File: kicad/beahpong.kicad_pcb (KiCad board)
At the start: 2 copper layers, 65 x 56 mm, 16 parts, among them J1 Conn_02x20_Odd_Even, J2 Conn_01x02, J3 Screw_Terminal_01x02, Q1 DMG2305UX, U1 CAT24C32, U2 DMMT5401

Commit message: Add level shifters
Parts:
- added C2: 100n, Capacitor_SMD:C_0402_1005Metric, F.Cu at (-20.9, -34.5)
- added C3: 100n, Capacitor_SMD:C_0402_1005Metric, F.Cu at (-22.0, -31.9)
- added C4: 100n, Capacitor_SMD:C_0402_1005Metric, F.Cu at (-26.0, -29.4)
- added R10: 680, Resistor_SMD:R_0603_1608Metric, F.Cu at (33.0, 39.5)
- added R11: 680, Resistor_SMD:R_0603_1608Metric, F.Cu at (-32.0, -44.2)
- added R12: 680, Resistor_SMD:R_0603_1608Metric, F.Cu at (35.0, 39.5)
- added R13: 680, Resistor_SMD:R_0603_1608Metric, F.Cu at (-36.4, -39.7)
- added R14: 680, Resistor_SMD:R_0603_1608Metric, F.Cu at (37.0, 39.5)
- added R15: 680, Resistor_SMD:R_0603_1608Metric, F.Cu at (-44.0, 15.0)
- added R16: 680, Resistor_SMD:R_0603_1608Metric, F.Cu at (39.0, 39.5)
- added R17: 680, Resistor_SMD:R_0603_1608Metric, F.Cu at (-32.4, -41.7)
- added R18: 680, Resistor_SMD:R_0603_1608Metric, F.Cu at (41.0, 39.5)
- added R19: 680, Resistor_SMD:R_0603_1608Metric, F.Cu at (-36.4, -37.2)
- added R20: 680, Resistor_SMD:R_0603_1608Metric, F.Cu at (43.0, 39.5)
- added R21: 680, Resistor_SMD:R_0603_1608Metric, F.Cu at (-44.0, 12.5)
- added R22: 200K, Resistor_SMD:R_0603_1608Metric, F.Cu at (43.5, 55.5)
- added R23: 200K, Resistor_SMD:R_0603_1608Metric, F.Cu at (-32.4, -39.2)
- added R24: 680, Resistor_SMD:R_0603_1608Metric, F.Cu at (41.5, 55.5)
- added R25: 680, Resistor_SMD:R_0603_1608Metric, F.Cu at (-19.0, 12.0)
- added R26: 680, Resistor_SMD:R_0603_1608Metric, F.Cu at (39.5, 55.5)
- added R27: 680, Resistor_SMD:R_0603_1608Metric, F.Cu at (-19.0, 14.0)
- added R28: 680, Resistor_SMD:R_0603_1608Metric, F.Cu at (37.5, 55.5)
- added R29: 680, Resistor_SMD:R_0603_1608Metric, F.Cu at (-24.0, -44.2)
- added R30: 680, Resistor_SMD:R_0603_1608Metric, F.Cu at (35.5, 55.5)
- added R31: 680, Resistor_SMD:R_0603_1608Metric, F.Cu at (-28.4, -39.2)
- added R32: 680, Resistor_SMD:R_0603_1608Metric, F.Cu at (33.5, 55.5)
- added R33: 680, Resistor_SMD:R_0603_1608Metric, F.Cu at (-24.0, 15.5)
- added R34: 680, Resistor_SMD:R_0603_1608Metric, F.Cu at (31.5, 55.5)
- added R35: 680, Resistor_SMD:R_0603_1608Metric, F.Cu at (-24.4, -41.7)
- added R36: 680, Resistor_SMD:R_0603_1608Metric, F.Cu at (29.5, 55.5)
- added R37: 680, Resistor_SMD:R_0603_1608Metric, F.Cu at (-28.4, -36.7)
- added R38: 680, Resistor_SMD:R_0603_1608Metric, F.Cu at (27.5, 55.5)
- added R39: 680, Resistor_SMD:R_0603_1608Metric, F.Cu at (-24.0, 17.5)
- added R40: 680, Resistor_SMD:R_0603_1608Metric, F.Cu at (-24.4, -39.2)
- added R41: 680, Resistor_SMD:R_0603_1608Metric, F.Cu at (-43.0, 6.50)
- added R42: 680, Resistor_SMD:R_0603_1608Metric, F.Cu at (-33.5, -29.2)
- added R43: 680, Resistor_SMD:R_0603_1608Metric, F.Cu at (-28.4, -34.2)
- added R44: 680, Resistor_SMD:R_0603_1608Metric, F.Cu at (-20.3, -41.7)
- added R45: 680, Resistor_SMD:R_0603_1608Metric, F.Cu at (-29.5, -31.7)
- added R46: 680, Resistor_SMD:R_0603_1608Metric, F.Cu at (-43.0, 4.50)
- added R47: 680, Resistor_SMD:R_0603_1608Metric, F.Cu at (-43.0, 2.50)
- added R48: 200K, Resistor_SMD:R_0603_1608Metric, F.Cu at (-15.0, -4.50)
- added R49: 680, Resistor_SMD:R_0603_1608Metric, F.Cu at (-20.3, -39.2)
- added R50: 680, Resistor_SMD:R_0603_1608Metric, F.Cu at (-15.0, 0.50)
- added R51: 680, Resistor_SMD:R_0603_1608Metric, F.Cu at (-15.0, 2.50)
- added R52: 680, Resistor_SMD:R_0603_1608Metric, F.Cu at (-24.4, -34.2)
- added R53: 680, Resistor_SMD:R_0603_1608Metric, F.Cu at (-15.0, 6.00)
- added R54: 680, Resistor_SMD:R_0603_1608Metric, F.Cu at (-25.5, -31.7)
- added R55: 680, Resistor_SMD:R_0603_1608Metric, F.Cu at (-20.3, -36.7)
- added R56: 680, Resistor_SMD:R_0603_1608Metric, F.Cu at (-23.5, 8.50)
- added R6: 680, Resistor_SMD:R_0603_1608Metric, F.Cu at (29.0, 39.5)
- added R7: 680, Resistor_SMD:R_0603_1608Metric, F.Cu at (-40.4, -38.7)
- added R8: 680, Resistor_SMD:R_0603_1608Metric, F.Cu at (31.0, 39.5)
- added R9: 680, Resistor_SMD:R_0603_1608Metric, F.Cu at (-44.0, 17.5)
- added U3: NVT2008PW, Package_SO:TSSOP-20_4.4x6.5mm_P0.65mm, F.Cu at (36.5, 47.5)
- added U4: NVT2008PW, Package_SO:TSSOP-20_4.4x6.5mm_P0.65mm, F.Cu at (-32.5, 14.5)
- added U5: NVT2008PW, Package_SO:TSSOP-20_4.4x6.5mm_P0.65mm, F.Cu at (-32.5, 4.00)
- J3: footprint Connector_Phoenix_MC:PhoenixContact_MCV_1,5_2-G-3.5_1x02_P3.50mm_Vertical -> Connector_Molex:Molex_KK-254_AE-6410-02A_1x02_P2.54mm_Vertical
- U1: value CAT24C32 -> DMMT5401; footprint Package_SO:SOIC-8_3.9x4.9mm_P1.27mm -> Package_TO_SOT_SMD:SOT-23-6
- U2: value DMMT5401 -> CAT24C32WI−GT3; footprint Package_TO_SOT_SMD:SOT-23-6 -> Package_SO:SOIC-8_3.9x4.9mm_P1.27mm
- moved U1 33.5 mm to (32.0, 30.0)
- moved U2 33.5 mm to (65.5, 29.5)
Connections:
- U1 pad 1: GND -> Net-(R4-Pad1)
- U1 pad 2: GND -> Net-(R4-Pad1)
- U1 pad 3: GND -> Net-(R4-Pad1)
- U1 pad 4: GND -> Net-(Q1-Pad1)
- U1 pad 5: /ID_SD -> +5V
- U1 pad 6: /ID_SC -> Net-(J3-Pad1)
- U2 pad 1: Net-(R4-Pad1) -> GND
- U2 pad 2: Net-(R4-Pad1) -> GND
- U2 pad 3: Net-(R4-Pad1) -> GND
- U2 pad 4: Net-(Q1-Pad1) -> GND
- U2 pad 5: +5V -> /ID_SD
- U2 pad 6: Net-(J3-Pad1) -> /ID_SC

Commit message: Finished layout of pcb
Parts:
- added J4: Conn_01x03, Connector_PinHeader_2.54mm:PinHeader_1x03_P2.54mm_Vertical, F.Cu at (77.5, 61.5)
- added J5: Conn_01x03, Connector_PinHeader_2.54mm:PinHeader_1x03_P2.54mm_Vertical, F.Cu at (77.5, 57.5)
- added J6: Conn_01x03, Connector_PinHeader_2.54mm:PinHeader_1x03_P2.54mm_Vertical, F.Cu at (77.5, 65.5)
- added J7: Conn_01x03, Connector_PinHeader_2.54mm:PinHeader_1x03_P2.54mm_Vertical, F.Cu at (77.5, 53.5)
- added J8: Conn_02x12_Odd_Even, Connector_PinHeader_2.54mm:PinHeader_2x12_P2.54mm_Vertical, F.Cu at (29.5, 72.5)
- J3: footprint Connector_Molex:Molex_KK-254_AE-6410-02A_1x02_P2.54mm_Vertical -> Connector_Phoenix_MC:PhoenixContact_MC_1,5_2-G-3.5_1x02_P3.50mm_Horizontal
- moved C4 134.5 mm to (84.2, 47.5), turned to 270 degrees
- moved R47 130.9 mm to (83.0, 38.0), turned to 270 degrees
- moved R45 129.4 mm to (79.5, 38.0), turned to 270 degrees
- moved R46 128.7 mm to (81.2, 38.0), turned to 270 degrees
- moved R23 128.6 mm to (57.8, 52.5), turned to 90 degrees
- moved R42 127.0 mm to (74.2, 38.0), turned to 270 degrees
- moved R55 126.9 mm to (73.8, 48.5), turned to 90 degrees
- moved R43 126.9 mm to (76.0, 38.0), turned to 270 degrees
- moved R44 126.4 mm to (77.8, 38.0), turned to 270 degrees
- moved R54 126.2 mm to (72.0, 48.5), turned to 90 degrees
- moved R52 124.3 mm to (68.5, 48.5), turned to 90 degrees
- moved R29 123.3 mm to (52.5, 52.5), turned to 90 degrees
- moved R40 122.5 mm to (70.8, 38.0), turned to 270 degrees
- moved R49 121.2 mm to (63.2, 48.5), turned to 90 degrees
- moved R31 121.1 mm to (50.8, 52.5), turned to 90 degrees
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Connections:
- net Net-(R24-Pad2) renamed /SENSOR_P2_3
- net Net-(R25-Pad2) renamed /SENSOR_P1_2
- net Net-(R26-Pad2) renamed /SENSOR_P1_6
- net Net-(R27-Pad2) renamed /SENSOR_P2_7
- net Net-(R28-Pad2) renamed /SENSOR_P2_2
- net Net-(R29-Pad2) renamed /SENSOR_P1_3
- net Net-(R30-Pad2) renamed /SENSOR_P1_7
- net Net-(R31-Pad2) renamed /SENSOR_P2_6
- net Net-(R32-Pad2) renamed /SENSOR_P2_1
- net Net-(R33-Pad2) renamed /SENSOR_P1_4
- net Net-(R34-Pad2) renamed /SENSOR_P1_8
- net Net-(R35-Pad2) renamed /SENSOR_P2_5
- net Net-(R36-Pad2) renamed /SENSOR_P2_0
- net Net-(R37-Pad2) renamed /SENSOR_P1_5
- net Net-(R38-Pad2) renamed /SENSOR_P1_9
- net Net-(R39-Pad2) renamed /SENSOR_P2_4
- net Net-(R49-Pad2) renamed /DOUT_M
- net Net-(R50-Pad2) renamed /DOUT_P1
- net Net-(R51-Pad2) renamed /DOUT_P2
- net Net-(R52-Pad2) renamed /RESERVED
- net Net-(R53-Pad2) renamed /SENSOR_P2_8
- net Net-(R54-Pad2) renamed /SENSOR_P1_1
- net Net-(R55-Pad2) renamed /SENSOR_P2_9
- net Net-(R56-Pad2) renamed /SENSOR_P1_0
- C2 pad 2: +5V -> Net-(C2-Pad2)
- C3 pad 2: +5V -> Net-(C3-Pad2)
- C4 pad 2: +5V -> Net-(C4-Pad2)
- J1 pad 10: (no net) -> /BCM15
- J1 pad 11: (no net) -> /BCM17
- J1 pad 12: (no net) -> /BCM18
- J1 pad 13: (no net) -> /BCM27
- J1 pad 15: (no net) -> /BCM22
- J1 pad 16: (no net) -> /BCM23
- J1 pad 18: (no net) -> /BCM24
- J1 pad 19: (no net) -> /BCM10
- J1 pad 21: (no net) -> /BCM9
- J1 pad 22: (no net) -> /BCM25
- J1 pad 23: (no net) -> /BCM11
- J1 pad 24: (no net) -> /BCM8
- J1 pad 3: (no net) -> /BCM2
- J1 pad 31: (no net) -> /BCM6
- J1 pad 32: (no net) -> /BCM12
- J1 pad 33: (no net) -> /BCM13
- J1 pad 35: (no net) -> /BCM19
- J1 pad 36: (no net) -> /BCM16
- J1 pad 37: (no net) -> /BCM26
- J1 pad 38: (no net) -> /BCM20
- J1 pad 40: (no net) -> /BCM21
- J1 pad 5: (no net) -> /BCM3
- J1 pad 7: (no net) -> /BCM4
- J1 pad 8: (no net) -> /BCM14
- R10 pad 2: Net-(R10-Pad2) -> /BCM4
- R11 pad 2: Net-(R11-Pad2) -> /BCM24
- R12 pad 2: Net-(R12-Pad2) -> /BCM14
- R13 pad 2: Net-(R13-Pad2) -> /BCM10
- R14 pad 2: Net-(R14-Pad2) -> /BCM15
- R15 pad 2: Net-(R15-Pad2) -> /BCM25
- R16 pad 2: Net-(R16-Pad2) -> /BCM17
- R17 pad 2: Net-(R17-Pad2) -> /BCM9
- R18 pad 2: Net-(R18-Pad2) -> /BCM18
- R19 pad 2: Net-(R19-Pad2) -> /BCM8
- R20 pad 2: Net-(R20-Pad2) -> /BCM27
- R21 pad 2: Net-(R21-Pad2) -> /BCM11
- R22 pad 2: Net-(R22-Pad2) -> Net-(C2-Pad2)
- R23 pad 2: Net-(R23-Pad2) -> Net-(C3-Pad2)
- R40 pad 2: Net-(R40-Pad2) -> /BCM6
- R41 pad 2: Net-(R41-Pad2) -> /BCM12
- R42 pad 2: Net-(R42-Pad2) -> /BCM13
- R43 pad 2: Net-(R43-Pad2) -> /BCM19
- R44 pad 2: Net-(R44-Pad2) -> /BCM16
- R45 pad 2: Net-(R45-Pad2) -> /BCM26
- R46 pad 2: Net-(R46-Pad2) -> /BCM20
- R47 pad 2: Net-(R47-Pad2) -> /BCM21
- R48 pad 2: Net-(R48-Pad2) -> Net-(C4-Pad2)
- R6 pad 2: Net-(R6-Pad2) -> /BCM2
- R7 pad 2: Net-(R7-Pad2) -> /BCM23
- R8 pad 2: Net-(R8-Pad2) -> /BCM3
- R9 pad 2: Net-(R9-Pad2) -> /BCM22
- U3 pad 10: Net-(R6-Pad2) -> /BCM2
- U3 pad 19: Net-(R22-Pad2) -> Net-(C2-Pad2)
- U3 pad 20: Net-(R22-Pad2) -> Net-(C2-Pad2)
- U3 pad 3: Net-(R20-Pad2) -> /BCM27
- U3 pad 4: Net-(R18-Pad2) -> /BCM18
- U3 pad 5: Net-(R16-Pad2) -> /BCM17
- U3 pad 6: Net-(R14-Pad2) -> /BCM15
- U3 pad 7: Net-(R12-Pad2) -> /BCM14
- U3 pad 8: Net-(R10-Pad2) -> /BCM4
- U3 pad 9: Net-(R8-Pad2) -> /BCM3
- U4 pad 10: Net-(R7-Pad2) -> /BCM23
- U4 pad 19: Net-(R23-Pad2) -> Net-(C3-Pad2)
- U4 pad 20: Net-(R23-Pad2) -> Net-(C3-Pad2)
- U4 pad 3: Net-(R21-Pad2) -> /BCM11
- U4 pad 4: Net-(R19-Pad2) -> /BCM8
- U4 pad 5: Net-(R17-Pad2) -> /BCM9
- U4 pad 6: Net-(R15-Pad2) -> /BCM25
- U4 pad 7: Net-(R13-Pad2) -> /BCM10
- U4 pad 8: Net-(R11-Pad2) -> /BCM24
- U4 pad 9: Net-(R9-Pad2) -> /BCM22
- U5 pad 10: Net-(R40-Pad2) -> /BCM6
- U5 pad 19: Net-(R48-Pad2) -> Net-(C4-Pad2)
- U5 pad 20: Net-(R48-Pad2) -> Net-(C4-Pad2)
- U5 pad 3: Net-(R47-Pad2) -> /BCM21
- U5 pad 4: Net-(R46-Pad2) -> /BCM20
- U5 pad 5: Net-(R45-Pad2) -> /BCM26
- U5 pad 6: Net-(R44-Pad2) -> /BCM16
- U5 pad 7: Net-(R43-Pad2) -> /BCM19
- U5 pad 8: Net-(R42-Pad2) -> /BCM13
- U5 pad 9: Net-(R41-Pad2) -> /BCM12
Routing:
- net +5V: track 16.9 -> 253.4 mm, vias 0 -> 30
- net +3V3: track 7.19 -> 143.3 mm, vias 0 -> 25
- net /DOUT_M: track 0.00 -> 44.8 mm
- net /SENSOR_P1_1: track 0.00 -> 41.4 mm
- net /SENSOR_P2_8: track 0.00 -> 40.7 mm
- net /DOUT_P1: track 0.00 -> 37.9 mm
- net /SENSOR_P2_9: track 0.00 -> 36.5 mm
- net /SENSOR_P1_0: track 0.00 -> 36.1 mm
- net /SENSOR_P1_9: track 0.00 -> 31.8 mm
- net /SENSOR_P1_5: track 0.00 -> 31.7 mm
- net /SENSOR_P1_8: track 0.00 -> 30.4 mm
- net /SENSOR_P1_4: track 0.00 -> 30.1 mm
- net /SENSOR_P2_4: track 0.00 -> 28.8 mm
- net /SENSOR_P2_0: track 0.00 -> 28.6 mm
- net /SENSOR_P1_3: track 0.00 -> 28.3 mm
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- added copper zone on B.Cu, net GND

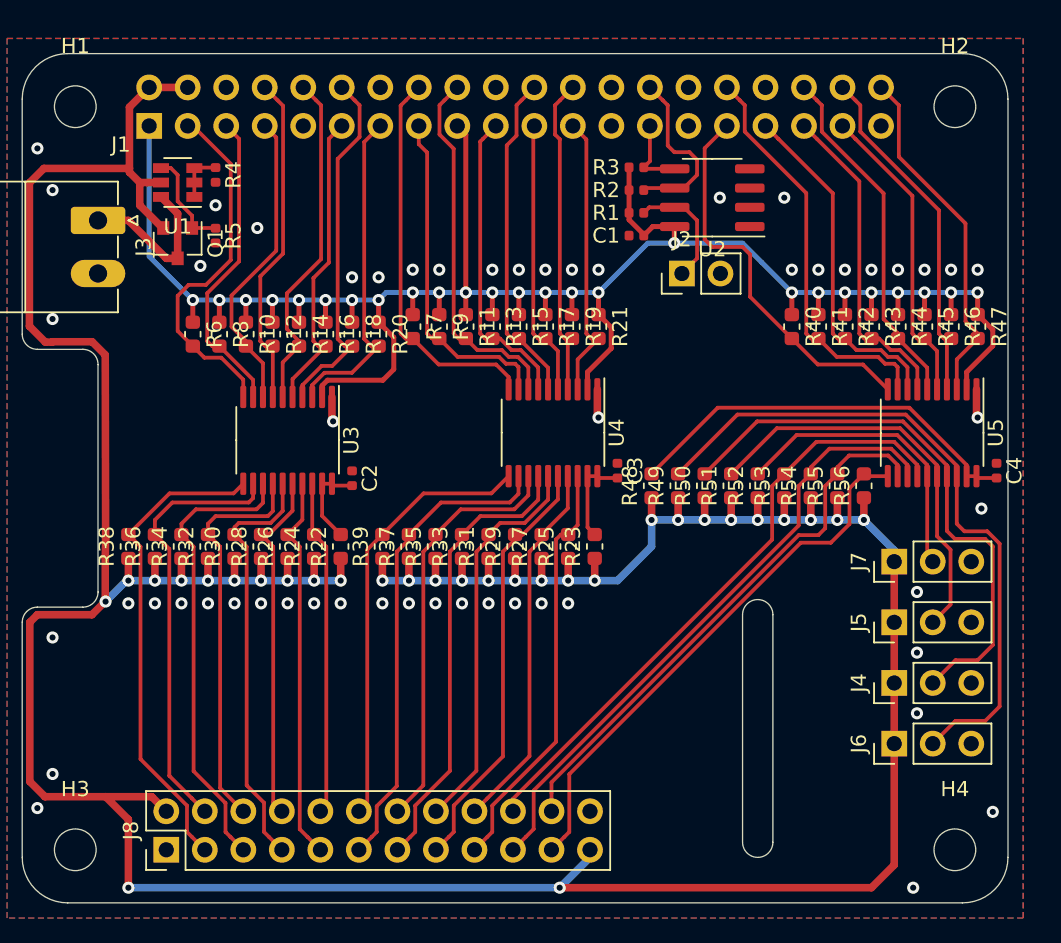
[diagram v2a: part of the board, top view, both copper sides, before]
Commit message: Change level shifter to one from LCSC database
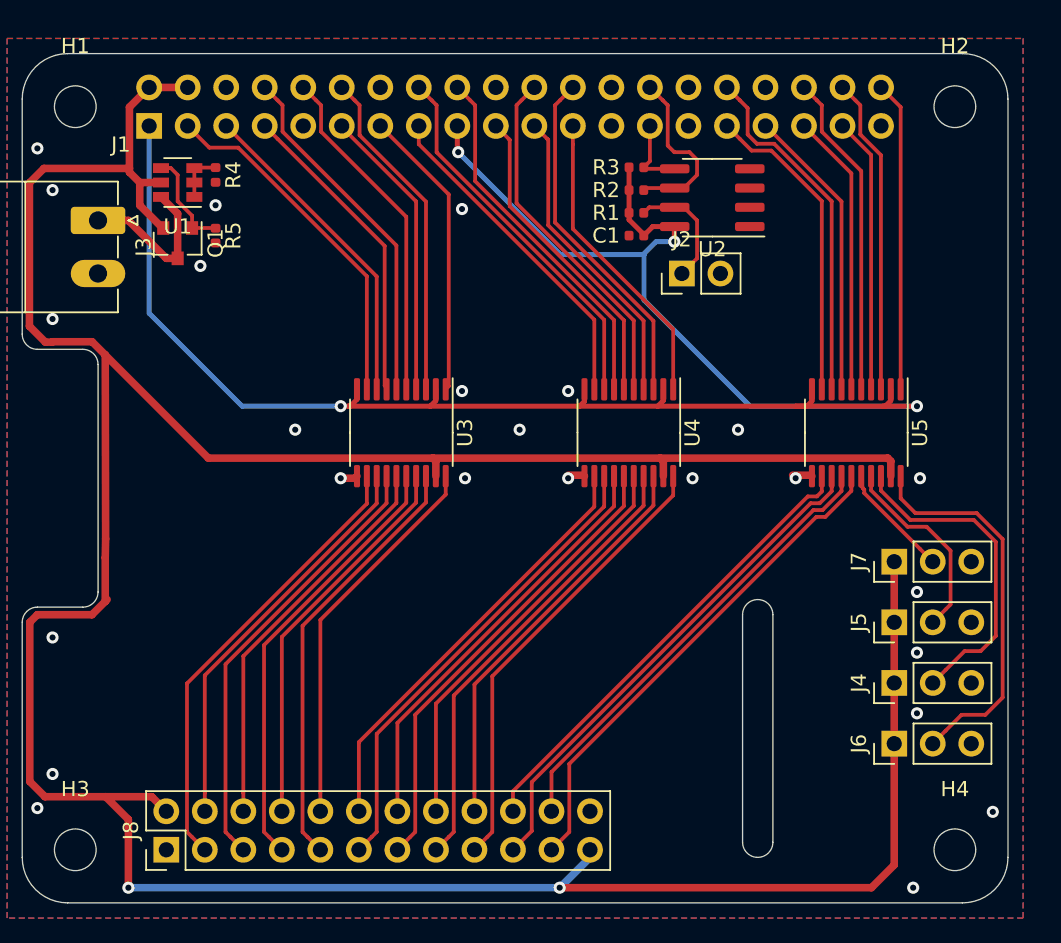
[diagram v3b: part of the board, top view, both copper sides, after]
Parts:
- removed C2, C3, C4: 100n, Capacitor_SMD:C_0402_1005Metric
- removed R10, R11, R12, R13, R14, R15, R16, R17, R18, R19, R20, R21, R24, R25, R26, R27, R28, R29, R30, R31, R32, R33, R34, R35, R36, R37, R38, R39, R40, R41, R42, R43, R44, R45, R46, R47, R49, R50, R51, R52, R53, R54, R55, R56, R6, R7, R8, R9: 680, Resistor_SMD:R_0603_1608Metric
- removed R22, R23, R48: 200K, Resistor_SMD:R_0603_1608Metric
- U3, U4, U5: value NVT2008PW -> TXS0108EPWR
- moved U3 7.52 mm to (45.0, 45.0)
- moved U4 5.00 mm to (60.0, 45.0)
- moved U5 5.00 mm to (75.0, 45.0)
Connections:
- U3 pad 1: GND -> /BCM27
- U3 pad 10: /BCM2 -> +3V3
- U3 pad 11: /SENSOR_P1_9 -> GND
- U3 pad 12: /SENSOR_P2_0 -> /SENSOR_P1_9
- U3 pad 13: /SENSOR_P1_8 -> /SENSOR_P2_0
- U3 pad 14: /SENSOR_P2_1 -> /SENSOR_P1_8
- U3 pad 15: /SENSOR_P1_7 -> /SENSOR_P2_1
- U3 pad 16: /SENSOR_P2_2 -> /SENSOR_P1_7
- U3 pad 17: /SENSOR_P1_6 -> /SENSOR_P2_2
- U3 pad 18: /SENSOR_P2_3 -> /SENSOR_P1_6
- U3 pad 19: Net-(C2-Pad2) -> +5V
- U3 pad 20: Net-(C2-Pad2) -> /SENSOR_P2_3
- U3 pad 3: /BCM27 -> /BCM18
- U3 pad 4: /BCM18 -> /BCM17
- U3 pad 5: /BCM17 -> /BCM15
- U3 pad 6: /BCM15 -> /BCM14
- U3 pad 7: /BCM14 -> /BCM4
- U3 pad 8: /BCM4 -> /BCM3
- U3 pad 9: /BCM3 -> /BCM2
- U4 pad 1: GND -> /BCM11
- U4 pad 10: /BCM23 -> +3V3
- U4 pad 11: /SENSOR_P2_4 -> GND
- U4 pad 12: /SENSOR_P1_5 -> /SENSOR_P2_4
- U4 pad 13: /SENSOR_P2_5 -> /SENSOR_P1_5
- U4 pad 14: /SENSOR_P1_4 -> /SENSOR_P2_5
- U4 pad 15: /SENSOR_P2_6 -> /SENSOR_P1_4
- U4 pad 16: /SENSOR_P1_3 -> /SENSOR_P2_6
- U4 pad 17: /SENSOR_P2_7 -> /SENSOR_P1_3
- U4 pad 18: /SENSOR_P1_2 -> /SENSOR_P2_7
- U4 pad 19: Net-(C3-Pad2) -> +5V
- U4 pad 20: Net-(C3-Pad2) -> /SENSOR_P1_2
- U4 pad 3: /BCM11 -> /BCM8
- U4 pad 4: /BCM8 -> /BCM9
- U4 pad 5: /BCM9 -> /BCM25
- U4 pad 6: /BCM25 -> /BCM10
- U4 pad 7: /BCM10 -> /BCM24
- U4 pad 8: /BCM24 -> /BCM23
- U5 pad 1: GND -> /BCM21
- U5 pad 10: /BCM6 -> +3V3
- U5 pad 11: /SENSOR_P1_0 -> GND
- U5 pad 12: /SENSOR_P2_9 -> /SENSOR_P2_8
- U5 pad 14: /SENSOR_P2_8 -> /SENSOR_P2_9
- U5 pad 15: /RESERVED -> /SENSOR_P1_0
- U5 pad 16: /DOUT_P2 -> /RESERVED
- U5 pad 17: /DOUT_P1 -> /DOUT_P2
- U5 pad 18: /DOUT_M -> /DOUT_P1
- U5 pad 19: Net-(C4-Pad2) -> +5V
- U5 pad 20: Net-(C4-Pad2) -> /DOUT_M
- U5 pad 3: /BCM21 -> /BCM20
- U5 pad 4: /BCM20 -> /BCM26
- U5 pad 5: /BCM26 -> /BCM16
- U5 pad 6: /BCM16 -> /BCM19
- U5 pad 7: /BCM19 -> /BCM13
- U5 pad 8: /BCM13 -> /BCM12
- U5 pad 9: /BCM12 -> /BCM6
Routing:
- net +5V: track 253.4 -> 218.0 mm, vias 30 -> 2
- net Net-(C4-Pad2): track 26.9 -> 0.00 mm
- net /DOUT_M: track 44.8 -> 25.6 mm
- net +3V3: track 143.3 -> 125.5 mm, vias 25 -> 4
- net /DOUT_P1: track 37.9 -> 21.6 mm
- net /DOUT_P2: track 27.0 -> 13.0 mm
- net /RESERVED: track 19.6 -> 7.59 mm
- net /SENSOR_P2_8: track 40.7 -> 30.9 mm
- net /SENSOR_P1_1: track 41.4 -> 33.7 mm
- net /SENSOR_P2_9: track 36.5 -> 30.4 mm
- net Net-(C3-Pad2): track 6.07 -> 0.00 mm
- net Net-(C2-Pad2): track 5.88 -> 0.00 mm
- net /BCM6: track 25.9 -> 20.7 mm
- net /SENSOR_P2_3: track 22.1 -> 25.5 mm
- net /BCM12: track 26.8 -> 23.4 mm
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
